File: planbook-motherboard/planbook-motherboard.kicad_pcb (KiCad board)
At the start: 6 copper layers, 151 x 88 mm, 441 parts, among them J1 CHARGER, J10 1-2199230-6, J11 Conn_01x33, J12 2199230-5, J13 3-2328724-1, J14 USB_C_Receptacle, J15 CONN_SPK, J16 SAMTEC_TSM-106-02-X-SH-A, J17 POWSW, J18 CONN_HEAD, J2 DM3AT-SF-PEJM5, J20 QWIIC, J3 USB_C_Receptacle, J4 09452812561, J5 SYSCTL, J6 USB_INT1, J7 HDMI_D_1.4, J8 SIM_Card, J9 Conn_01x20, SW1 SW_DIP_x01, SW2 RESET, SW3 RESET, U1 reform2-som-connector, U10 W25Q32JVSS, U11 PCF8523T, U12 AP22615AWU-7, U13 TXS0108EPW, U14 SN74AVC1T45, U15 TPD4E02B04DQA, U16 TPD4E02B04DQA, U17 TPD12S521, U18 TLV320AIC3100, U19 TPD4E02B04DQA, U2 TS3USB30EDGSR, U20 TPD4E02B04DQA, U21 TPD4E02B04DQA, U22 TPD4E02B04DQA, U23 FUSB302BMPX, U24 TXS0108EPW, U25 TUSB8041, U27 TVS2200DRV, U28 LM62460, U29 AP22615AWU-7, U3 LM2830XQMFE/NOPB, U30 TS3USB30EDGSR, U31 TS3USB30EDGSR, U32 AP22615AWU-7, U33 AT24CS02-STUM, U34 PCA9536DP, U35 TMUXHS4446RETR, U36 AP22615AWU-7, U37 TS3USB30EDGSR, U38 CY7C65215-32LTXI, U39 PCA9557PW, U4 TLV75718PDBV, U40 AP22615AWU-7, U41 AP22615AWU-7, U42 TPS560430X3FDBVR, U5 LM73100RPWR, U6 LM62460, U7 74LVC1G34, U8 RP2040, U9 TPS7A0533PDBZ, Y1 24MHz, Y2 12MHz 12pF, Y3 32.768 kHz

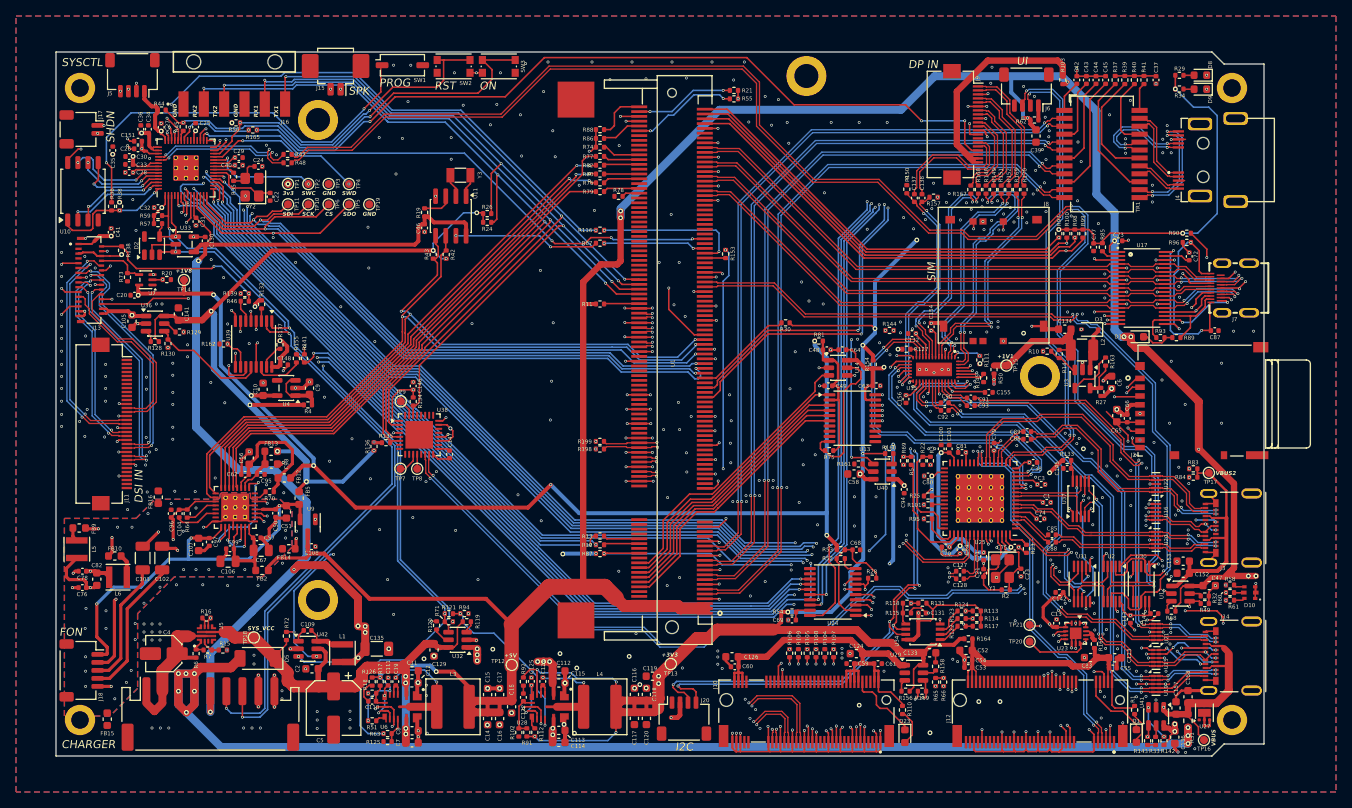
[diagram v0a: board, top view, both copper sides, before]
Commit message: Phase 2 & 3: PCB performance improvements and implementation guides
Implemented:
- Added ground stitching vias around board edges (214 vias total across 4 PCBs)
  - planbook-motherboard: 48 vias (10mm spacing)
  - planbook-charger: 26 vias (8mm spacing)
  - planbook-keyboard-kailh-ortho: 76 vias (8mm spacing)
  - planbook-wifi: 64 vias (5mm spacing)
- Via specifications: 0.3mm drill, 0.6mm diameter, connected to GND
- Improves EMI performance and grounding

Created comprehensive implementation guides:
- PHASE2_DECOUPLING_GUIDE.md: RP2040 decoupling capacitor recommendations
- PHASE2_ESD_PROTECTION_GUIDE.md: ESD protection for USB, SD card, keyboard, etc.
- PHASE3_THERMAL_MANAGEMENT_GUIDE.md: Thermal via recommendations for hot components
- PHASE3_COPPER_POUR_GUIDE.md: Copper pour improvements for heat dissipation
- PHASE3_LED_OPTIMIZATION_GUIDE.md: LED current limiting resistor optimization
- GROUND_STITCHING_VIAS_SUMMARY.md: Summary of ground stitching via additions

Guides require KiCad GUI implementation for component additions and modifications.

Generated with [Devin](https://devin.ai)

Co-Authored-By: Devin <158243242+devin-ai-integration[bot]@users.noreply.github.com>
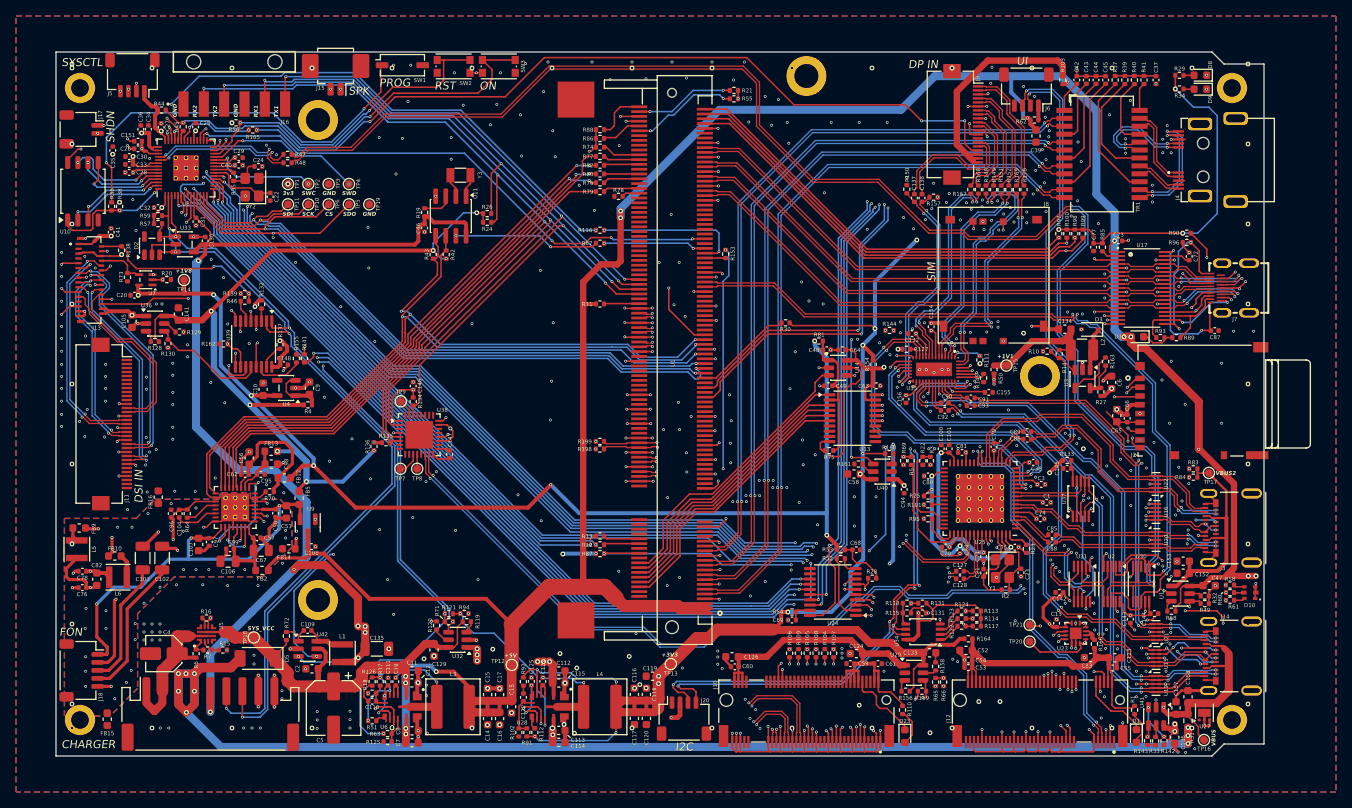
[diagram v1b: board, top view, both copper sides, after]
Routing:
- net GND: vias 634 -> 682
